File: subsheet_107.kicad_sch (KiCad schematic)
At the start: 27 parts, among them T12 BDX54

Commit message: update comments in cartridge
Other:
- title: Conversion du Thomson MO5 — Unité centrale v1 -> Conversion du Thomson MO5 — Unité centrale v2
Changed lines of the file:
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@@
   (paper "A4" portrait)
   (title_block
-    (title "Conversion du Thomson MO5 — Unité centrale v1")
-    (date "2024-12-30")
-    (rev "v1.0.0-rc2")
+    (title "Conversion du Thomson MO5 — Unité centrale v2")
+    (date "2025-02-08")
+    (rev "v2.0.0-alpha")
     (comment 1 "http://github.com/sporniket/kicad-conversions--thomson-mo5--v1")
-    (comment 3 "Gate Array Motorola MCA 1300 ALS")
-    (comment 4 "Reference : POP5001 501994-01")
+    (comment 3 "Gate Array EFCIS")
   )
   (junction (at 38.1 147.32) (diameter 0) (color 0 0 0 0)

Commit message: start reworking power supply
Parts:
- I54: value L78L05_TO92 -> L78L12_TO220; footprint Package_TO_SOT_THT:TO-92_Inline_Wide -> Package_TO_SOT_THT:TO-220-3_Vertical; symbol Regulator_Linear:L78L05_TO92 -> power-custom:MC78Lxx_TO220
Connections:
- net +18V: now also I54.1 (VI); no longer I54.3 (VI)
- net at C54.1, R81.1: now also I54.3 (VO); no longer I54.1 (VO)
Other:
- note added: "Source +18V"
- moved on the sheet: C53, C54, C55, C56, D07, F01, H1, H2, H3, H4, H5, H6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

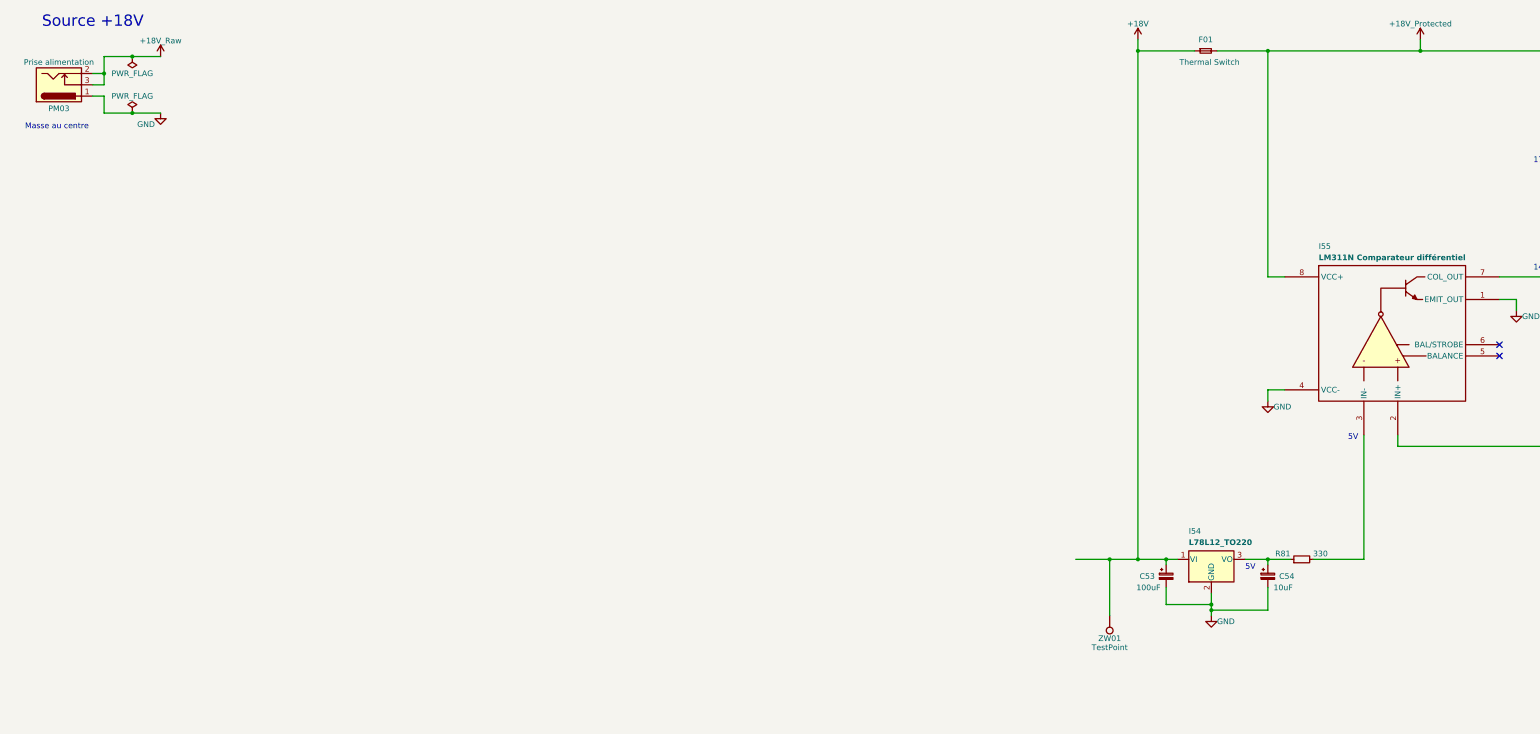
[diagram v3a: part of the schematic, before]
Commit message: power supply : 18V, 12V
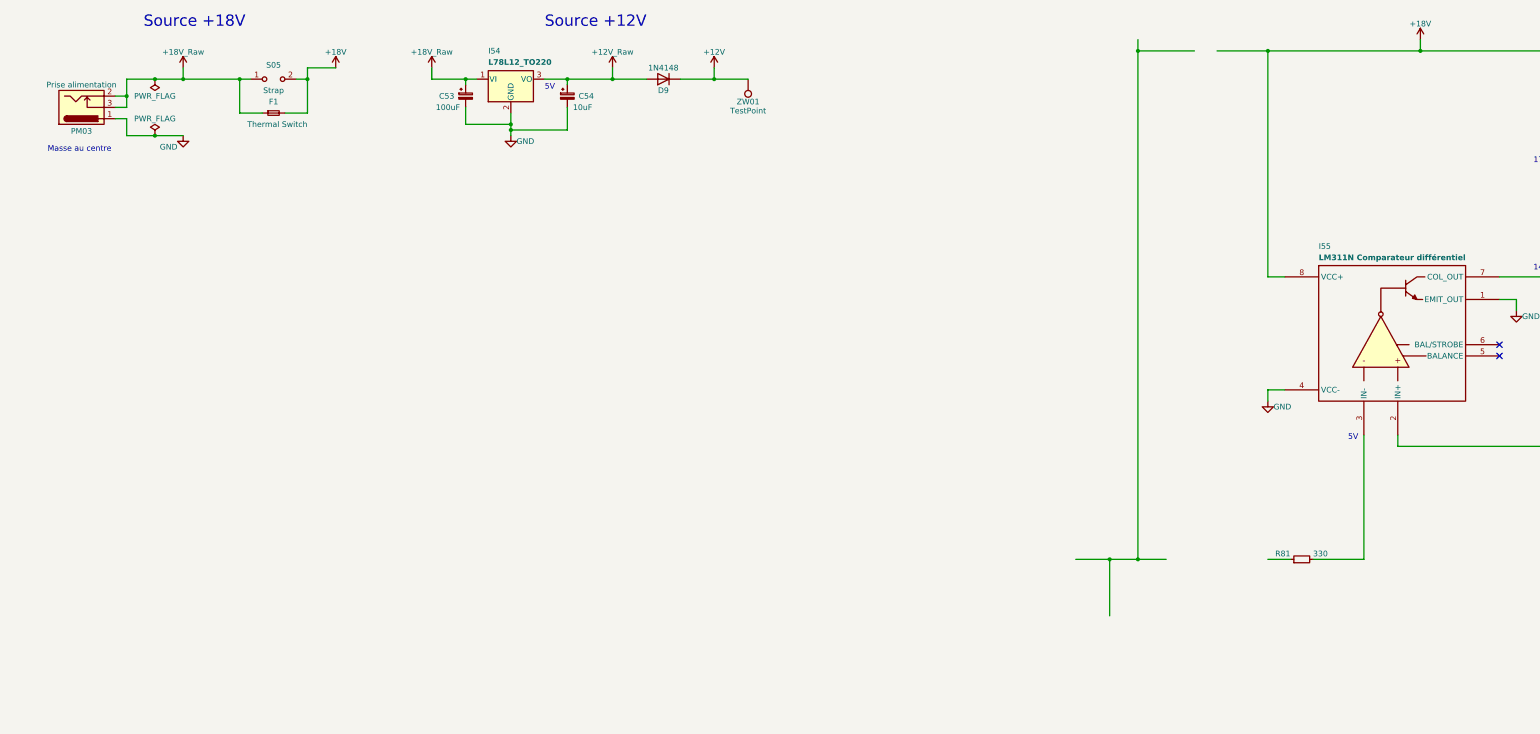
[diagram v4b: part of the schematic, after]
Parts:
- removed F01: Thermal Switch, thomson-moto-passives:Passive_THT_thermal_switch_L5.08mm, symbol Device:Fuse_Small
- added D9: 1N4148, Diode_THT:D_DO-35_SOD27_P7.62mm_Horizontal, symbol Diode:1N4148
- added F1: Thermal Switch, thomson-moto-passives:Passive_THT_thermal_switch_L5.08mm, symbol Device:Fuse_Small
- added S05: Strap, symbol custom_passives:Strap
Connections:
- net +18V_Protected is gone; now on net +18V: I55.8 (VCC+), R78.1, T12.3 (E)
- net +18V: now also C54.1, I54.3 (VO), D9.1 (K), D9.2 (A), F1.1, F1.2, S05.1 (A), S05.2 (B)
- now unconnected: R81.1
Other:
- note added: "Source +12V"
- moved on the sheet: C53, C54, I54, PM03, ZW01

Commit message: start doing the +5V circuit
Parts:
- added J7: Jumper wire, symbol Connector_Generic:Conn_01x02
- added P2: 1K, Potentiometer_THT:Potentiometer_ACP_CA9-V10_Vertical_Hole, symbol Device:R_Potentiometer
- added R89: 1K3, commons-passives_THT:Passive_THT_resistor_EU_W2.54mm_L12.70mm, symbol Device:R_Small
- added R90: 1K, commons-passives_THT:Passive_THT_resistor_EU_W2.54mm_L12.70mm, symbol Device:R_Small
- added R93: 0.47, commons-passives_THT:Passive_THT_resistor_EU_W2.54mm_L12.70mm, symbol Device:R_Small
- renumbered R80 to R91
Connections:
- net +18V: now also R89.1
- net GND: now also R90.2
- net at L02.2, L03.1, R83.2: now also R93.1; no longer C55.1
- net at R81.1: now also R89.2, R90.1
- net at I55.7 (COL_OUT), R79.2: now also J7.1 (Pin_1), P2.1, P2.2; no longer R91.1
- new net: C55.1, R93.2
- new net: J7.2 (Pin_2), P2.3, R91.1
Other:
- moved on the sheet: C55, C56, D07, HS1, I55, L02, L03, R78, R79, R81, R83, R91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

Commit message: continue the +5V circuit
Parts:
- removed D9: 1N4148, Diode_THT:D_DO-35_SOD27_P7.62mm_Horizontal, symbol Diode:1N4148
- added D11, D13: 1N4148, commons-passives_THT:Passive_THT_diode_W2.54mm_L12.70mm, symbol Device:D_Small
- added R87, R88: 4K7, commons-passives_THT:Passive_THT_resistor_EU_W2.54mm_L12.70mm, symbol Device:R_Small
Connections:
- net +18V: now also D13.1 (K), D13.2 (A)
- net +5V: now also R88.2
- net GND: now also D11.2 (A)
- net at D07.1 (K), HS1.1 (Pin_1), HS1.2 (Pin_2)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: now also R87.1
- new net: D11.1 (K), R87.2, R88.1
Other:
- moved on the sheet: D07, HS1, L02

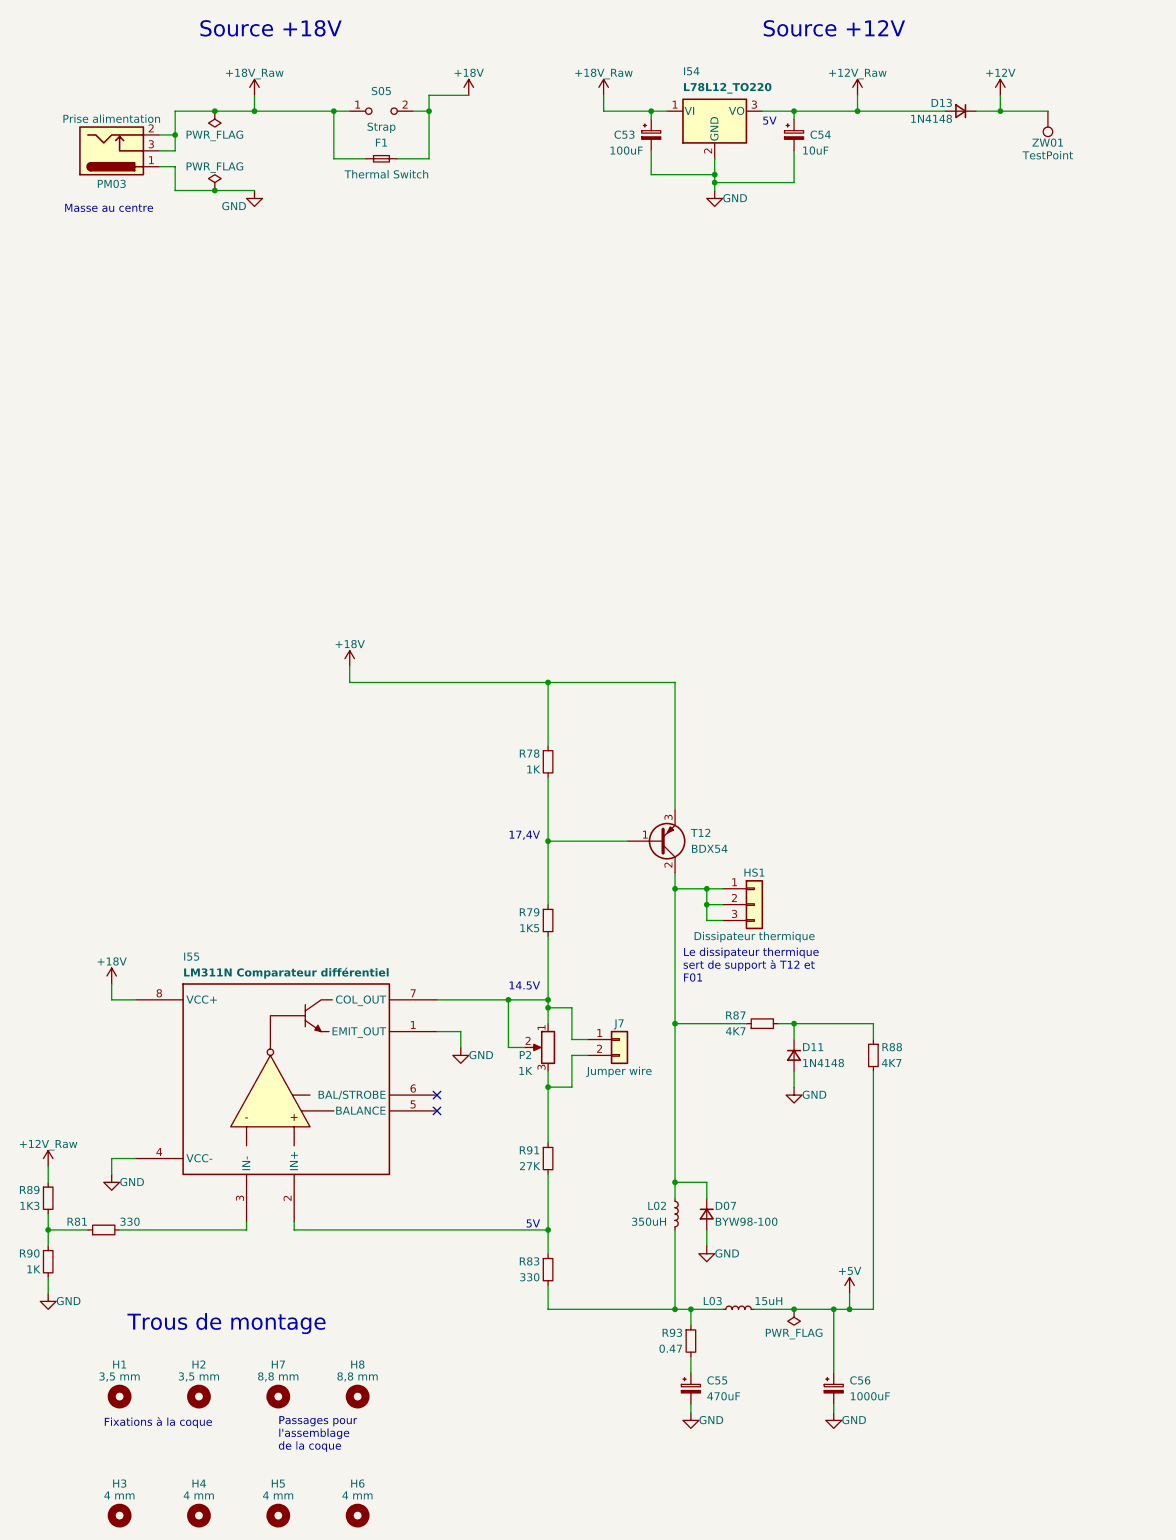
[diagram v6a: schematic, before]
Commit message: done power supply circuit
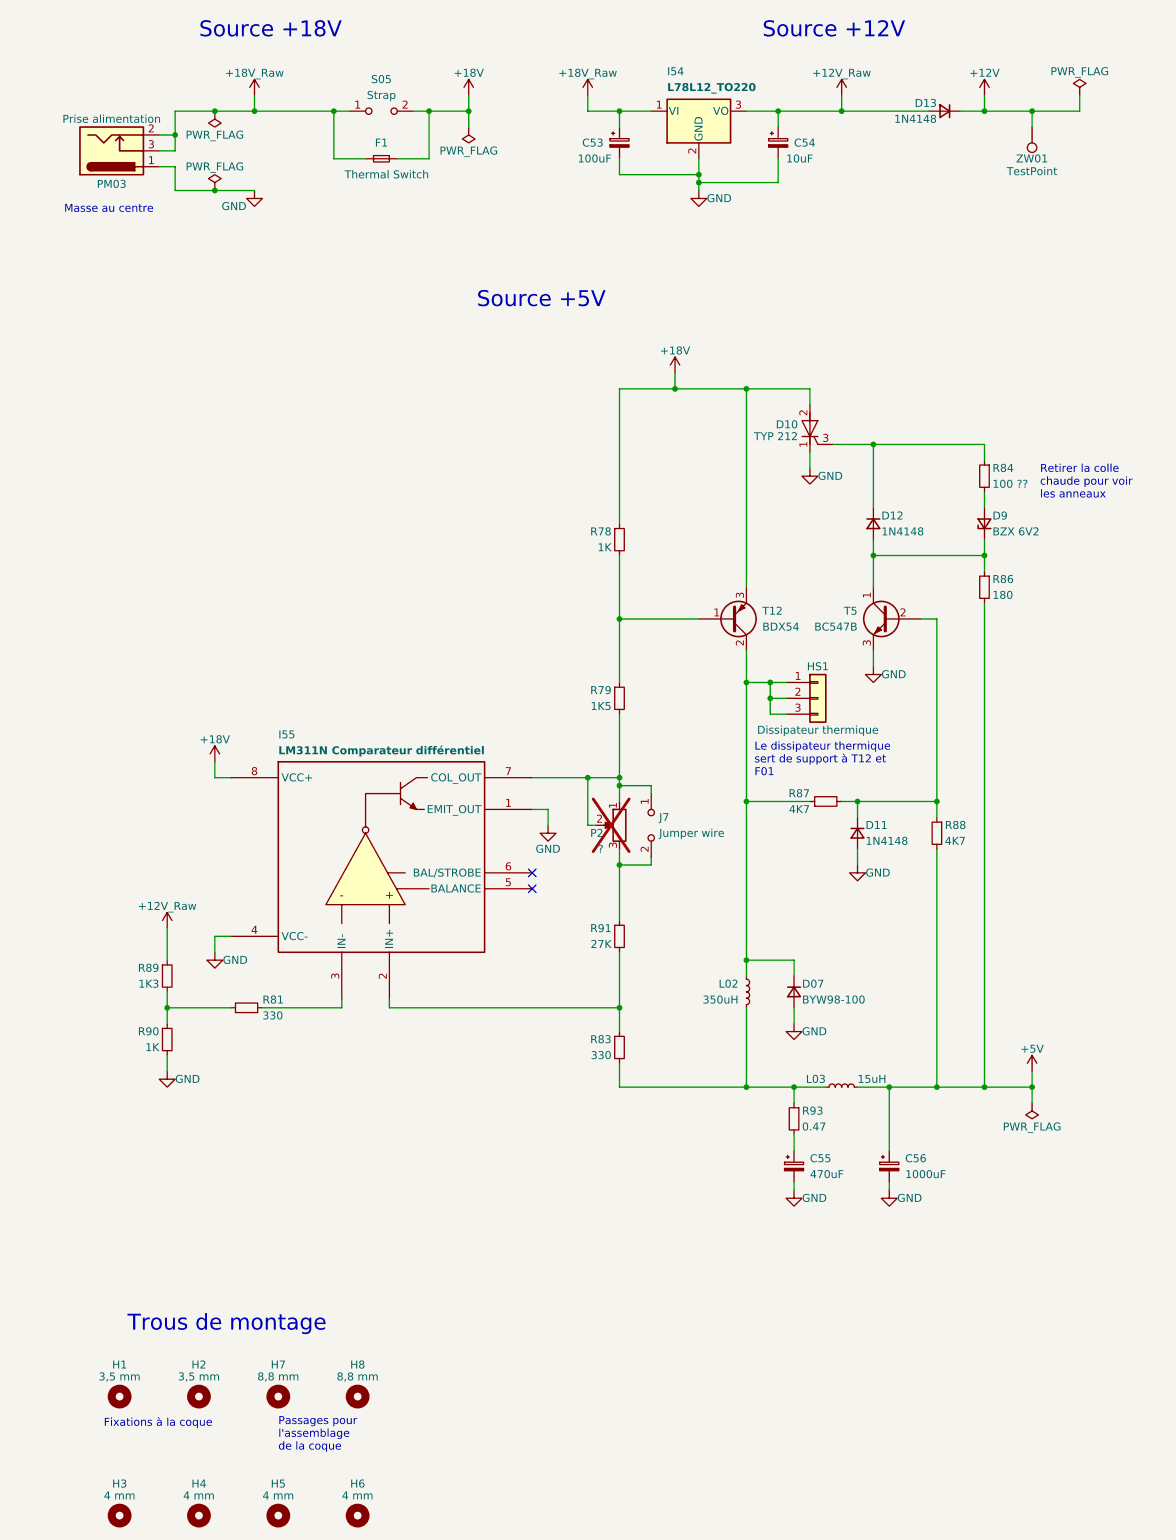
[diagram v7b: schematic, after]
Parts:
- added D10: TYP 212, symbol Device:Q_SCR_KAG
- added D12: 1N4148, commons-passives_THT:Passive_THT_diode_W2.54mm_L12.70mm, symbol Device:D_Small
- added D9: BZX 6V2, symbol Device:D_Zener_Small
- added R84: 100 ??, commons-passives_THT:Passive_THT_resistor_EU_W2.54mm_L12.70mm, symbol Device:R_Small
- added R86: 180, commons-passives_THT:Passive_THT_resistor_EU_W2.54mm_L12.70mm, symbol Device:R_Small
- added T5: BC547B, Package_TO_SOT_THT:TO-92_Inline_Wide, symbol Device:Q_NPN_CBE
- J7: symbol Connector_Generic:Conn_01x02 -> custom_passives:Strap
- P2: value 1K -> ?; now not fitted
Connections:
- net +18V: now also D10.2 (A)
- net +5V: now also R86.2
- net GND: now also D10.1 (K), T5.3 (E)
- net at D11.1 (K), R87.2, R88.1: now also T5.2 (B)
- new net: D12.2 (A), D9.1 (K), R86.1, T5.1 (C)
- new net: D9.2 (A), R84.2
- new net: D10.3 (G), D12.1 (K), R84.1
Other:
- note added: "Retirer la colle chaude pour voir les anneaux"
- note added: "Source +5V"
- note removed: "14.5V"
- note removed: "17,4V"
- note removed: "5V"
- moved on the sheet: C53, C54, C55, C56, D07, D11, D13, HS1, I54, I55, L02, L03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

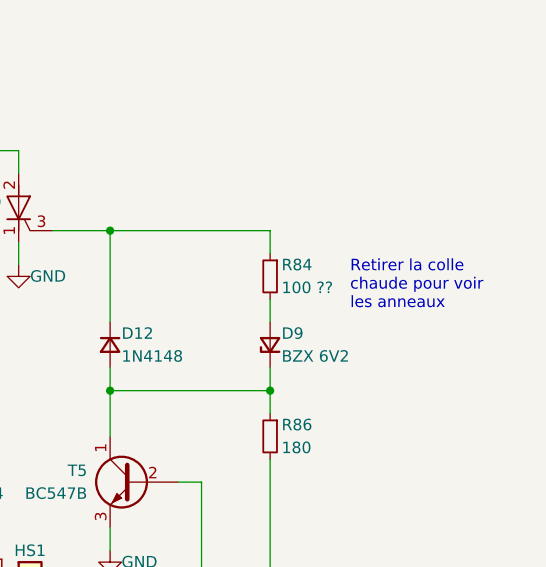
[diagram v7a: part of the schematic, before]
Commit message: Confirmed value of R84 : 100
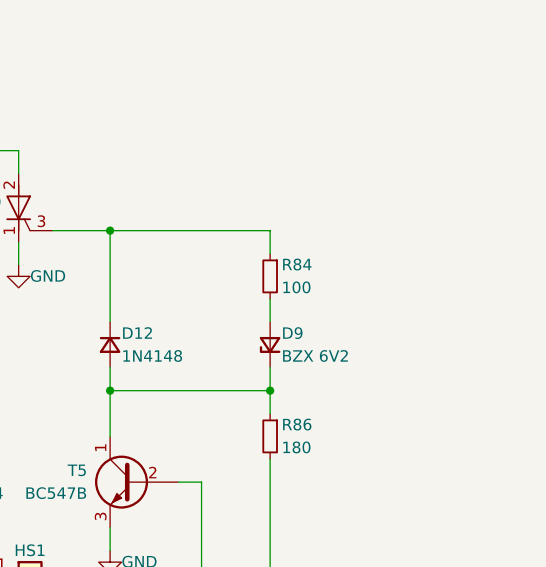
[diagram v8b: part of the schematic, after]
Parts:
- R84: value 100 ?? -> 100
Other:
- note removed: "Retirer la colle chaude pour voir les anneaux"
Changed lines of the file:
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@@
-    (effects (font (size 1.27 1.27)) (justify left bottom))
-  )
-  (text "Retirer la colle\nchaude pour voir\nles anneaux" (at 179.07 93.98 0)
     (effects (font (size 1.27 1.27)) (justify left bottom))
   )
@@
       (effects (font (size 1.27 1.27)) (justify right))
     )
-    (property "Value" "100 ??" (at 171.45 91.44 0)
-      (effects (font (size 1.27 1.27)) (justify right))
-    )
+    (property "Value" "100" (at 171.45 91.44 0)
+      (effects (font (size 1.27 1.27)) (justify right))
+    )
